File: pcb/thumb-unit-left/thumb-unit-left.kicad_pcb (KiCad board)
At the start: 2 copper layers, 82.5 x 79 mm, 24 parts, among them J1 Conn_01x10, SW1 SW_SPDT, SW2 SW_Push, SW3 SW_Push, SW4 SW_Push, SW5 SW_Push, U1 xiao-ble, U2 PMW3610, U3 TLV70218_SOT23-5

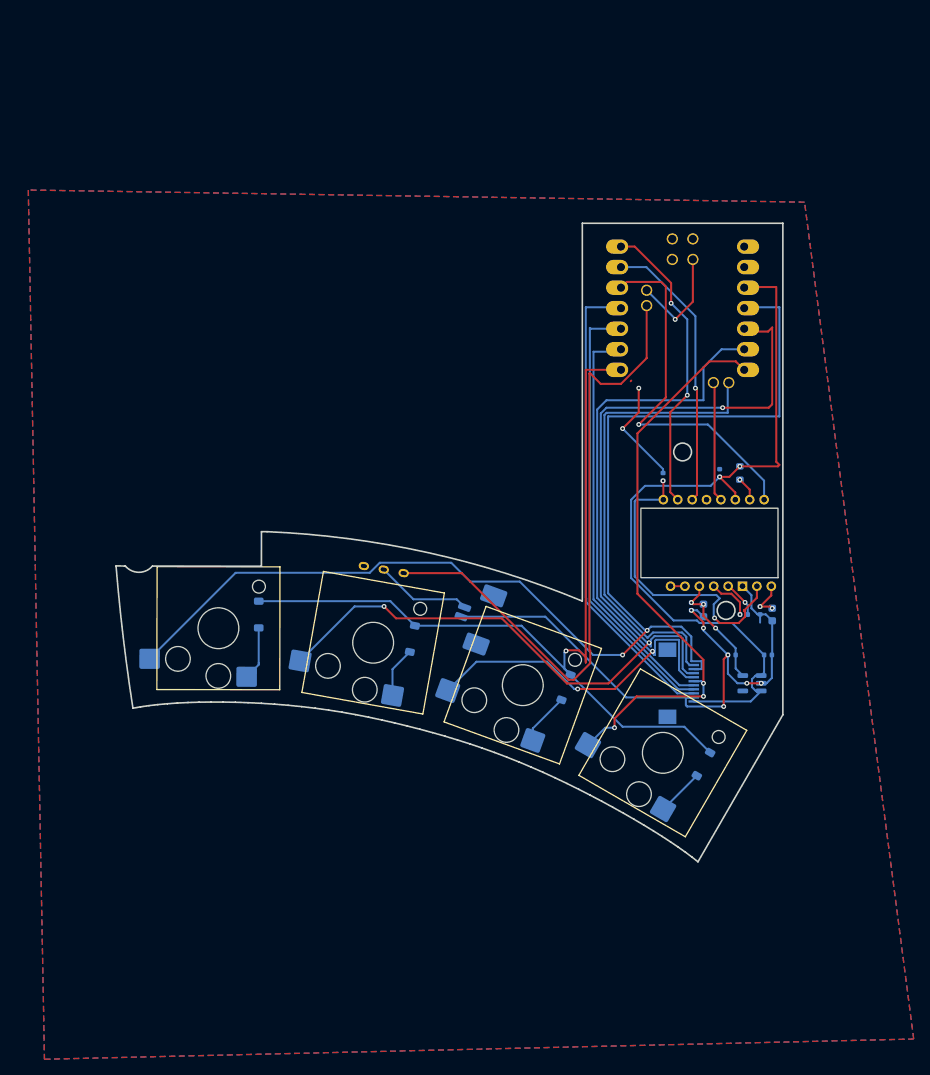
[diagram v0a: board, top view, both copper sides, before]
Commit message: fix(pcb/thumb-unit-left): GND pour, swap to roBa XIAO footprint, clean routing
- Schematic: switch U1 footprint to mcu_roba:XIAO_nRF52840_wBAT_wNFC_1
  to match the right half (same schematic file structure; the two
  halves only differ in PCB).
- PCB: add B.Cu GND zone (SMD side for the left half is the bottom
  layer) and remove F.Cu↔B.Cu stitching vias that were blocking the
  zone from reaching C2 / J1 / U3 GND pads.
- PCB: route +3V3, +1V8, the SPI bus (SDIO/SCLK/MOTION/NCS), the
  keyboard matrix (ROW0-3 × COL0-4), the trackball charge-pump and
  VCSEL nets, and the BAT_SW power switch path so all nets resolve.

DRC: 0 unconnected, 0 schematic-parity errors. Remaining warnings are
identical in kind to the right half (environment-only and intentional
edge clearances on U1 pads 19-22).

Co-Authored-By: Claude Opus 4.7 (1M context) <noreply@anthropic.com>
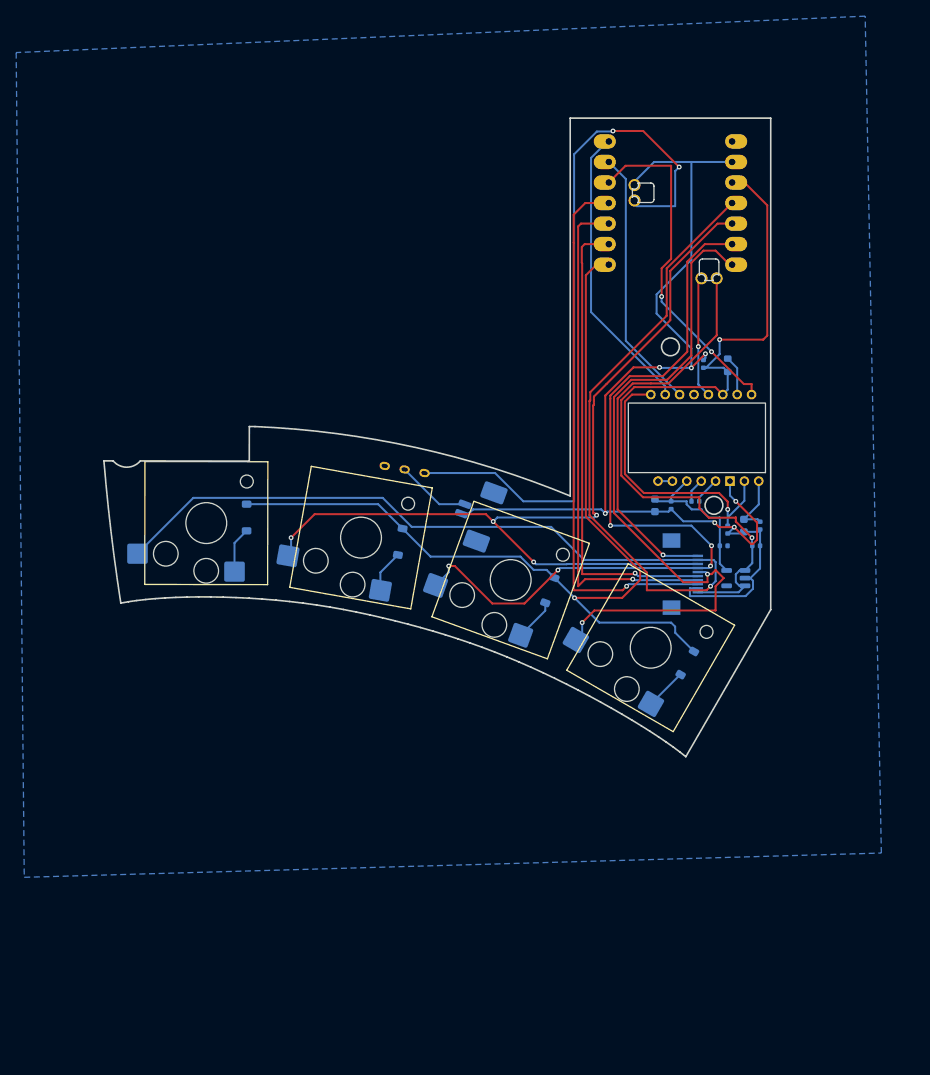
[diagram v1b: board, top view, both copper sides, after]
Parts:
- U1: footprint mcu:xiao-ble-tht -> mcu_roba:XIAO_nRF52840_wBAT_wNFC_1
- moved U1 23.6 mm to (173.9, 63.6)
- moved C13 15.2 mm to (177.0, 111.0)
- moved C17 14.3 mm to (172.0, 111.5)
- moved C15 13.6 mm to (178.0, 94.0)
- moved C1 13.6 mm to (184.5, 116.5)
- moved C2 13.5 mm to (180.5, 116.5), turned to 180 degrees
- moved J1 13.5 mm to (175.4, 120.0)
- moved R1 13.4 mm to (181.0, 94.2), turned to 90 degrees
- moved U3 13.2 mm to (182.0, 120.5)
- moved U2 13.1 mm to (175.8, 103.2)
- moved SW2 13.1 mm to (171.5, 129.1)
- moved SW3 13.1 mm to (154.2, 120.7)
- moved SW5 13.1 mm to (116.5, 113.7)
- moved SW4 13.1 mm to (135.6, 115.5)
- moved C16 12.8 mm to (174.0, 111.5)
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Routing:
- net GND: track 105.7 -> 144.5 mm, vias 9 -> 7
- net /COL0: track 72.0 -> 87.9 mm, vias 3 -> 2
- net /COL2: track 128.8 -> 114.1 mm, vias 3 -> 4
- net /COL4: track 58.3 -> 48.6 mm, vias 0 -> 1
- net /BAT_SW: track 80.6 -> 89.5 mm, vias 0 -> 2
- net /ROW1: track 55.0 -> 63.7 mm, vias 0 -> 1
- net /ROW0: track 58.9 -> 67.0 mm, vias 0 -> 1
- net /ROW2: track 50.9 -> 58.5 mm, vias 0 -> 1
- net /COL3: track 152.7 -> 147.1 mm, vias 2 -> 1
- net /ROW3: track 111.0 -> 116.2 mm
- net +1V8: track 14.9 -> 19.5 mm, vias 3 -> 0
- net Net-(U2-VCP): track 4.68 -> 8.25 mm, vias 2 -> 0
- net Net-(U2-+VCSEL): track 38.5 -> 35.0 mm, vias 2 -> 1
- net /COL1: track 97.9 -> 100.8 mm, vias 2 -> 5
- net /MOTION: track 45.2 -> 42.5 mm, vias 1 -> 2
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- removed copper zone on F.Cu, net GND
